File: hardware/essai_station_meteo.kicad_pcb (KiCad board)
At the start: 2 copper layers, 151 x 82 mm, 41 parts, among them J1 Bornier Alim, J2 ESP32-PICO-KIT-V4.1, J3 SD_Card, J4 Pluviometre, J5 Aneno/Girou, J6 Bornier Capteurs, J8 Debug_link, Q1 BS170, SW1 SW_Push, SW2 SW_Push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

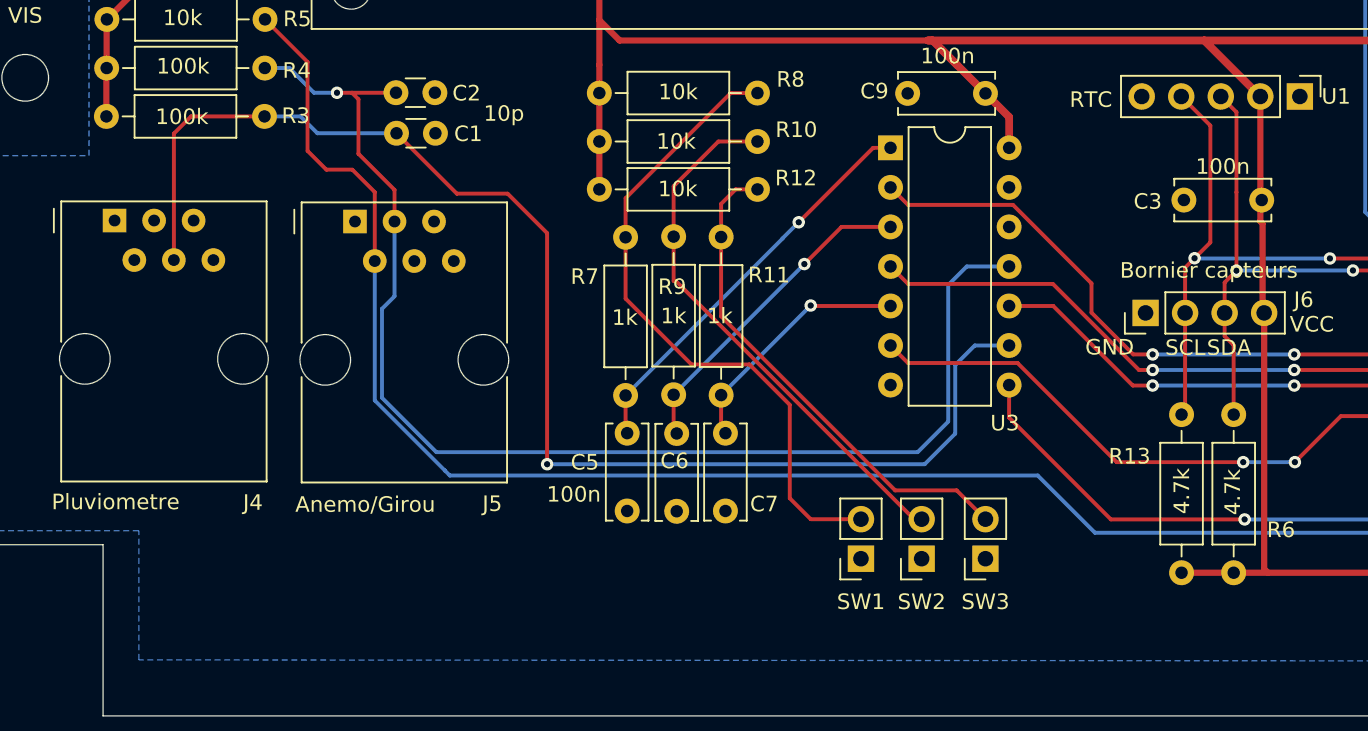
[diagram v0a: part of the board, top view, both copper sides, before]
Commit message: add name of board + move capa to avoid RTC collision
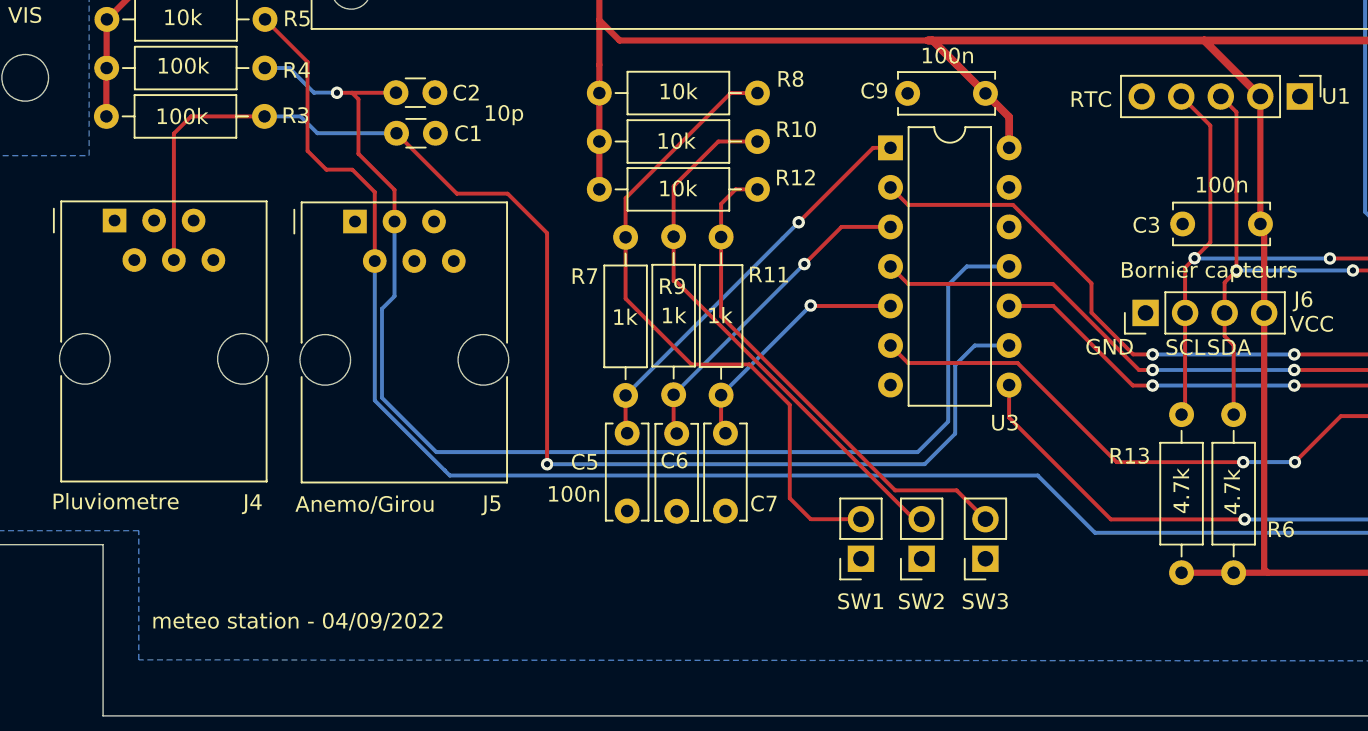
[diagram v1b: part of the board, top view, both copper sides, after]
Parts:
- moved C3 1.54 mm to (114.4, 70.4)
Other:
- board text added: "meteo station - 04/09/2022"
